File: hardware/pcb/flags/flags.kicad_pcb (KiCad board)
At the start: 2 copper layers, 62.2 x 21.6 mm, 42 parts, among them J1 Bus, J2 Control, J3 Sync, J4 Power, J5 Flags_Bus, J6 Ctrl_Out, U1 74HC02, U2 74HC08, U3 74HC157, U4 74HC173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

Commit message: Reorder flag bits on bus
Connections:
- U3 pad 11: CARRY_IN -> OV_IN
- U3 pad 12: Z_I -> C_I
- U3 pad 13: BUS0 -> BUS2
- U3 pad 14: Z_OUT -> CARRY_IN
- U3 pad 3: BUS2 -> BUS0
- U3 pad 5: OV_IN -> Z_OUT
- U3 pad 7: V_I -> Z_I
- U3 pad 9: C_I -> V_I
- U6 pad 12: C_D -> V_D
- U6 pad 2: Z_D -> N_D
- U6 pad 5: V_D -> Z_D
- U6 pad 9: N_D -> C_D
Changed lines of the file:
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@@
       (net 2 GND))
     (pad 14 smd rect (at 3.55 1.905) (size 1.5 0.6) (layers B.Cu B.Paste B.Mask)
-      (net 19 Z_OUT))
+      (net 22 CARRY_IN))
     (pad 13 smd rect (at 3.55 0.635) (size 1.5 0.6) (layers B.Cu B.Paste B.Mask)
-      (net 11 BUS0))
+      (net 9 BUS2))
     (pad 12 smd rect (at 3.55 -0.635) (size 1.5 0.6) (layers B.Cu B.Paste B.Mask)
-      (net 45 Z_I))
+      (net 46 C_I))
     (pad 11 smd rect (at 3.55 -1.905) (size 1.5 0.6) (layers B.Cu B.Paste B.Mask)
-      (net 22 CARRY_IN))
+      (net 21 OV_IN))
     (pad 10 smd rect (at 3.55 -3.175) (size 1.5 0.6) (layers B.Cu B.Paste B.Mask)
       (net 8 BUS3))
     (pad 9 smd rect (at 3.55 -4.445) (size 1.5 0.6) (layers B.Cu B.Paste B.Mask)
-      (net 46 C_I))
+      (net 47 V_I))
     (pad 8 smd rect (at -3.55 -4.445) (size 1.5 0.6) (layers B.Cu B.Paste B.Mask)
       (net 2 GND))
     (pad 7 smd rect (at -3.55 -3.175) (size 1.5 0.6) (layers B.Cu B.Paste B.Mask)
-      (net 47 V_I))
+      (net 45 Z_I))
     (pad 6 smd rect (at -3.55 -1.905) (size 1.5 0.6) (layers B.Cu B.Paste B.Mask)
       (net 10 BUS1))
     (pad 5 smd rect (at -3.55 -0.635) (size 1.5 0.6) (layers B.Cu B.Paste B.Mask)
-      (net 21 OV_IN))
+      (net 19 Z_OUT))
     (pad 4 smd rect (at -3.55 0.635) (size 1.5 0.6) (layers B.Cu B.Paste B.Mask)
       (net 48 N_I))
     (pad 3 smd rect (at -3.55 1.905) (size 1.5 0.6) (layers B.Cu B.Paste B.Mask)
-      (net 9 BUS2))
+      (net 11 BUS0))
     (pad 2 smd rect (at -3.55 3.175) (size 1.5 0.6) (layers B.Cu B.Paste B.Mask)
       (net 4 BUS7))
@@
       (net 12 ~OUT~))
     (pad 2 smd rect (at -2.7 -2.54 270) (size 1.5 0.6) (layers F.Cu F.Paste F.Mask)
-      (net 31 Z_D))
+      (net 33 N_D))
     (pad 3 smd rect (at -2.7 -1.27 270) (size 1.5 0.6) (layers F.Cu F.Paste F.Mask)
       (net 11 BUS0))
@@
       (net 12 ~OUT~))
     (pad 5 smd rect (at -2.7 1.27 270) (size 1.5 0.6) (layers F.Cu F.Paste F.Mask)
-      (net 32 V_D))
+      (net 31 Z_D))
     (pad 6 smd rect (at -2.7 2.54 270) (size 1.5 0.6) (layers F.Cu F.Paste F.Mask)
       (net 10 BUS1))
@@
       (net 9 BUS2))
     (pad 9 smd rect (at 2.7 2.54 270) (size 1.5 0.6) (layers F.Cu F.Paste F.Mask)
-      (net 33 N_D))
+      (net 34 C_D))
     (pad 10 smd rect (at 2.7 1.27 270) (size 1.5 0.6) (layers F.Cu F.Paste F.Mask)
       (net 12 ~OUT~))
@@
       (net 8 BUS3))
     (pad 12 smd rect (at 2.7 -1.27 270) (size 1.5 0.6) (layers F.Cu F.Paste F.Mask)
-      (net 34 C_D))
+      (net 32 V_D))
     (pad 13 smd rect (at 2.7 -2.54 270) (size 1.5 0.6) (layers F.Cu F.Paste F.Mask)
       (net 12 ~OUT~))

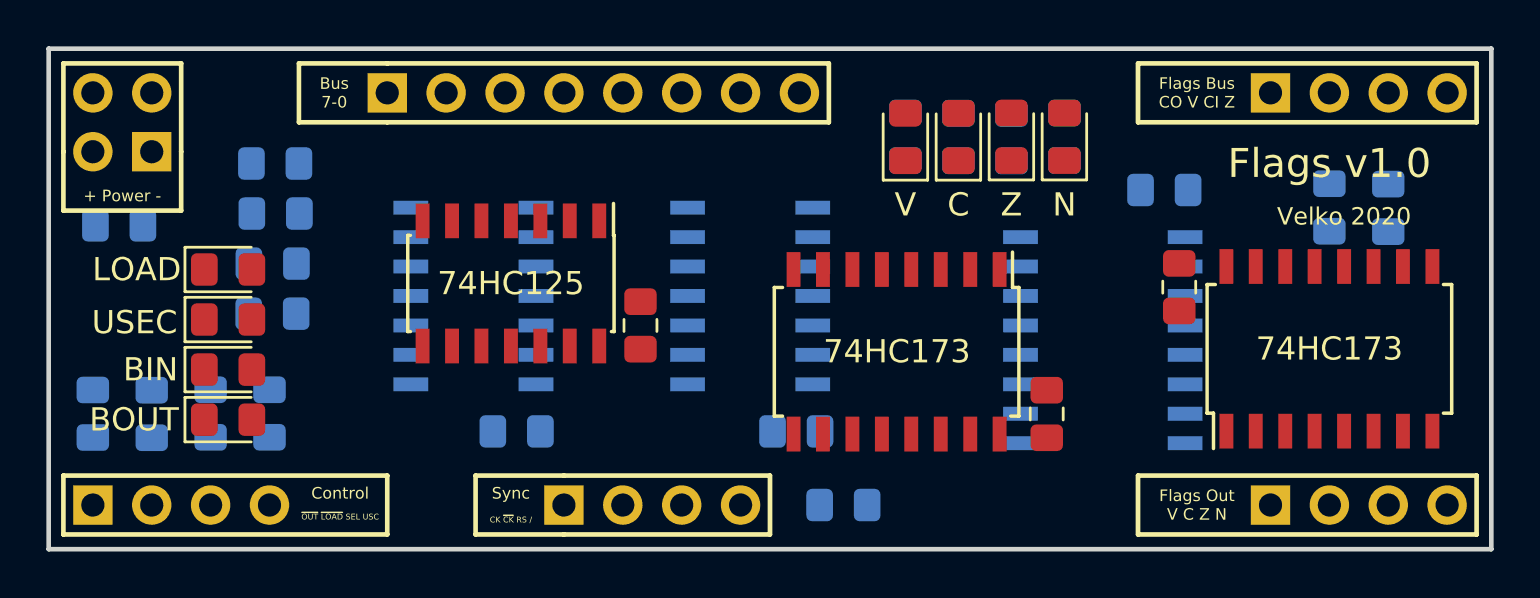
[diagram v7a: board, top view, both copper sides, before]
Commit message: Import autorouted
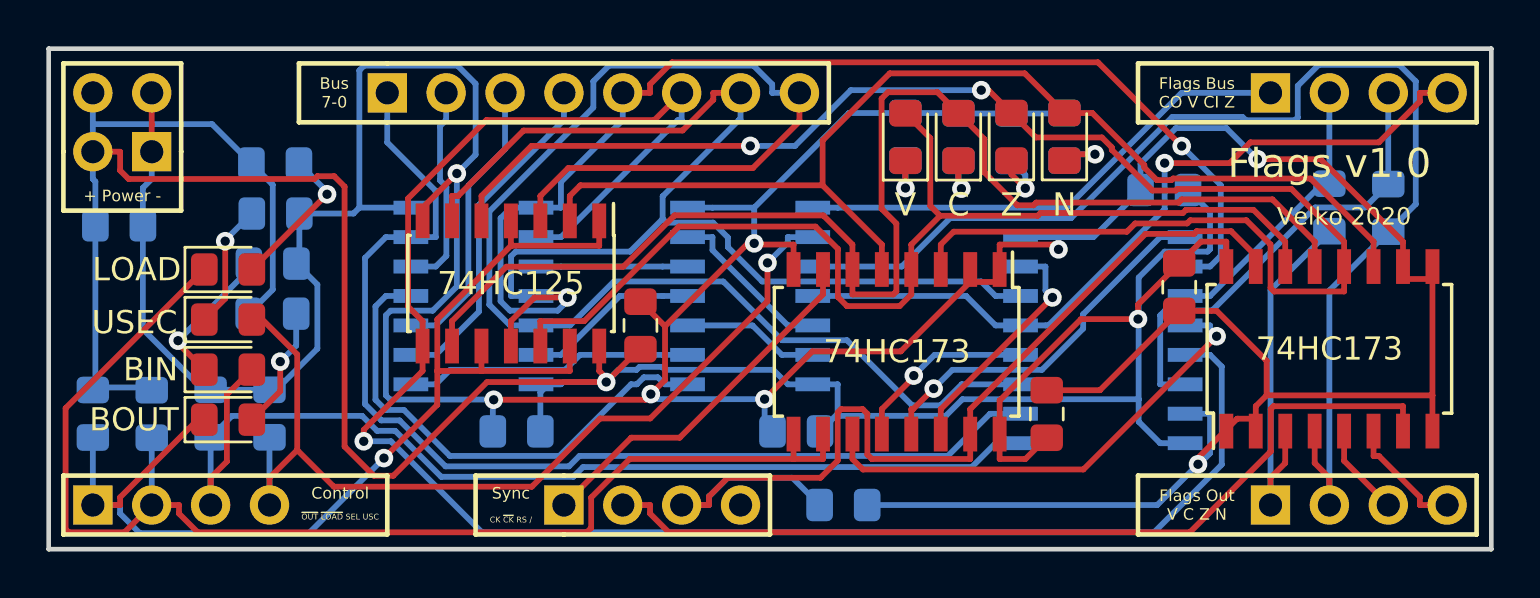
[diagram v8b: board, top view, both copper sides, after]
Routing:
- net GND: track 0.00 -> 205.7 mm, vias 0 -> 8
- net VCC: track 0.00 -> 136.3 mm, vias 0 -> 2
- net BUS2: track 0.00 -> 80.9 mm, vias 0 -> 1
- net Z_D: track 0.00 -> 66.4 mm, vias 0 -> 2
- net BUS0: track 0.00 -> 62.8 mm
- net C_D: track 0.00 -> 57.0 mm
- net ~LOAD~: track 0.00 -> 54.7 mm
- net C_CTRL: track 0.00 -> 54.1 mm
- net BUS3: track 0.00 -> 53.3 mm, vias 0 -> 2
- net BUS1: track 0.00 -> 49.5 mm
- net ~OUT~: track 0.00 -> 49.3 mm, vias 0 -> 1
- net N_D: track 0.00 -> 48.0 mm
- net V_D: track 0.00 -> 47.2 mm
- net BUS7: track 0.00 -> 47.1 mm
- net SEL: track 0.00 -> 46.5 mm
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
